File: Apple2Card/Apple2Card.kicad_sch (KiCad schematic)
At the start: 57 parts, among them J1 ICSP, J2 Conn_01x25, J3 Conn_01x25, J4 Conn_01x16, J5 SERCON, J6 WIZNET 5500, SW1 SW_Push, U1 ATmega328P-P, U3 74HCT00, U4 82C55A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

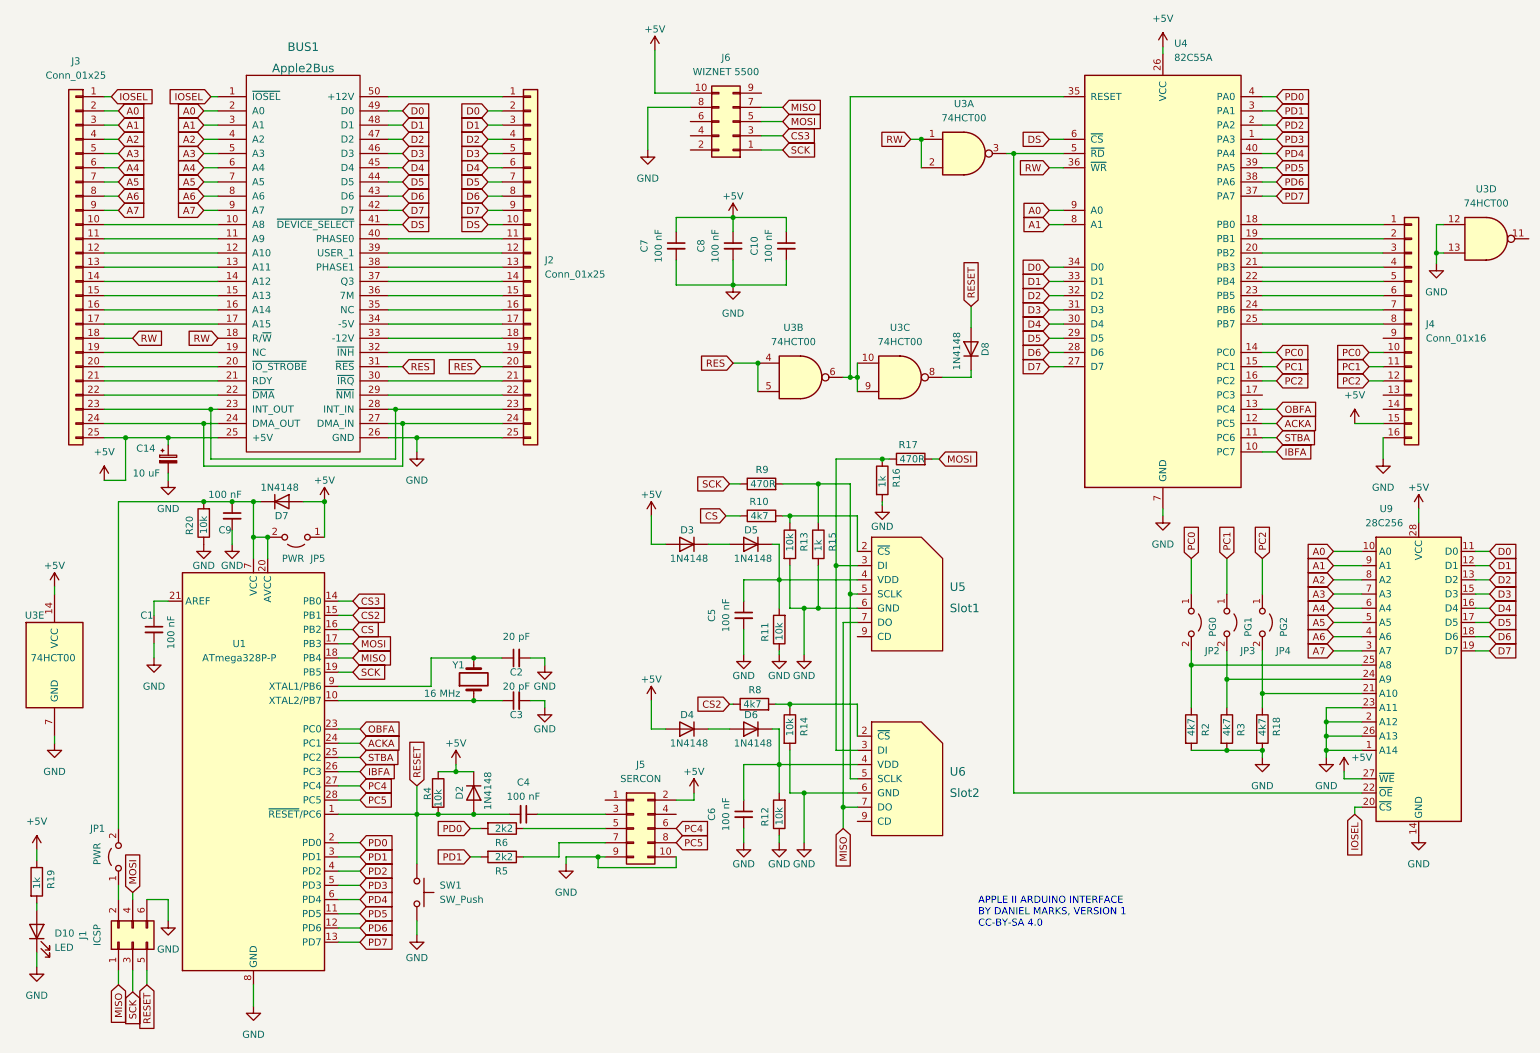
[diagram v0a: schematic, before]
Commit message: Fixed device select timing bug
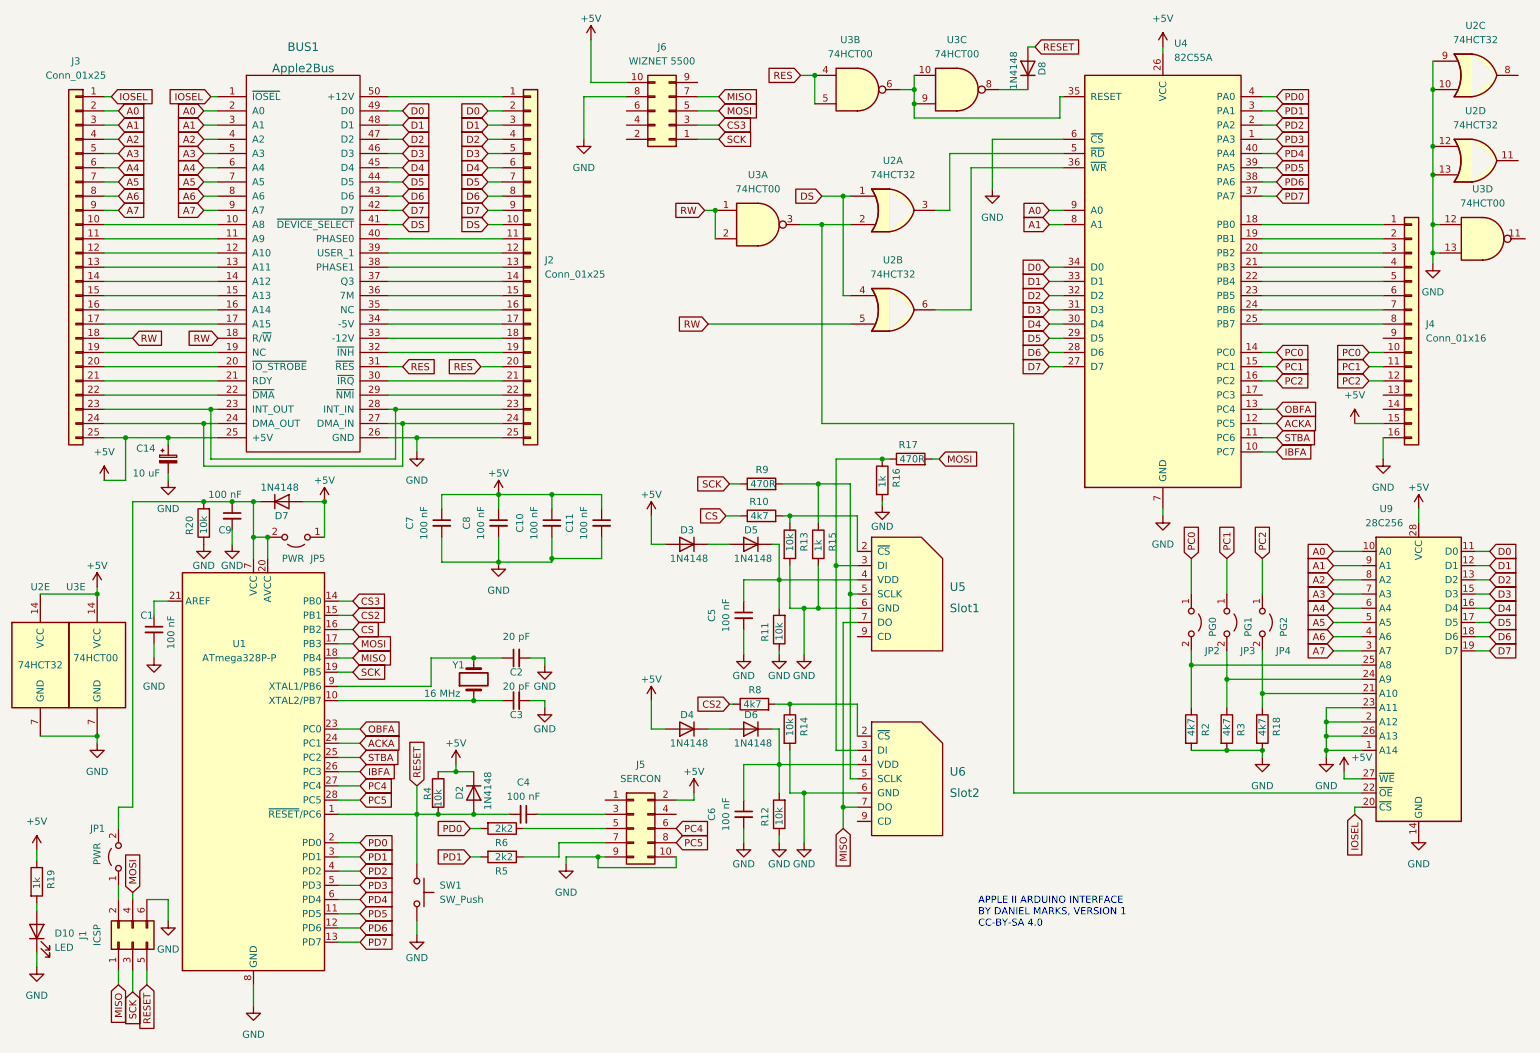
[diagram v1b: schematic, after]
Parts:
- added C11: 100 nF, Capacitor_THT:C_Disc_D5.0mm_W2.5mm_P5.00mm, symbol Device:C_Small
- added U2: 74HCT32, Package_DIP:DIP-14_W7.62mm_Socket, symbol 74xx:74LS32
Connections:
- net +5V: now also C11.1, U2.14 (VCC)
- net DS: now also U2.1, U2.4; no longer U4.6 (~{CS})
- net GND: now also U4.6 (~{CS}), C11.2, U2.10, U2.12, U2.13, U2.7 (GND), U2.9
- net RW: now also U2.5; no longer U4.36 (~{WR})
- net at U3.3, U9.22 (~{OE}): now also U2.2; no longer U4.5 (~{RD})
- new net: U2.3, U4.5 (~{RD})
- new net: U2.6, U4.36 (~{WR})
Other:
- moved on the sheet: C10, C7, C8, D8, J6, U3A, U3B, U3C, U3D, U3E

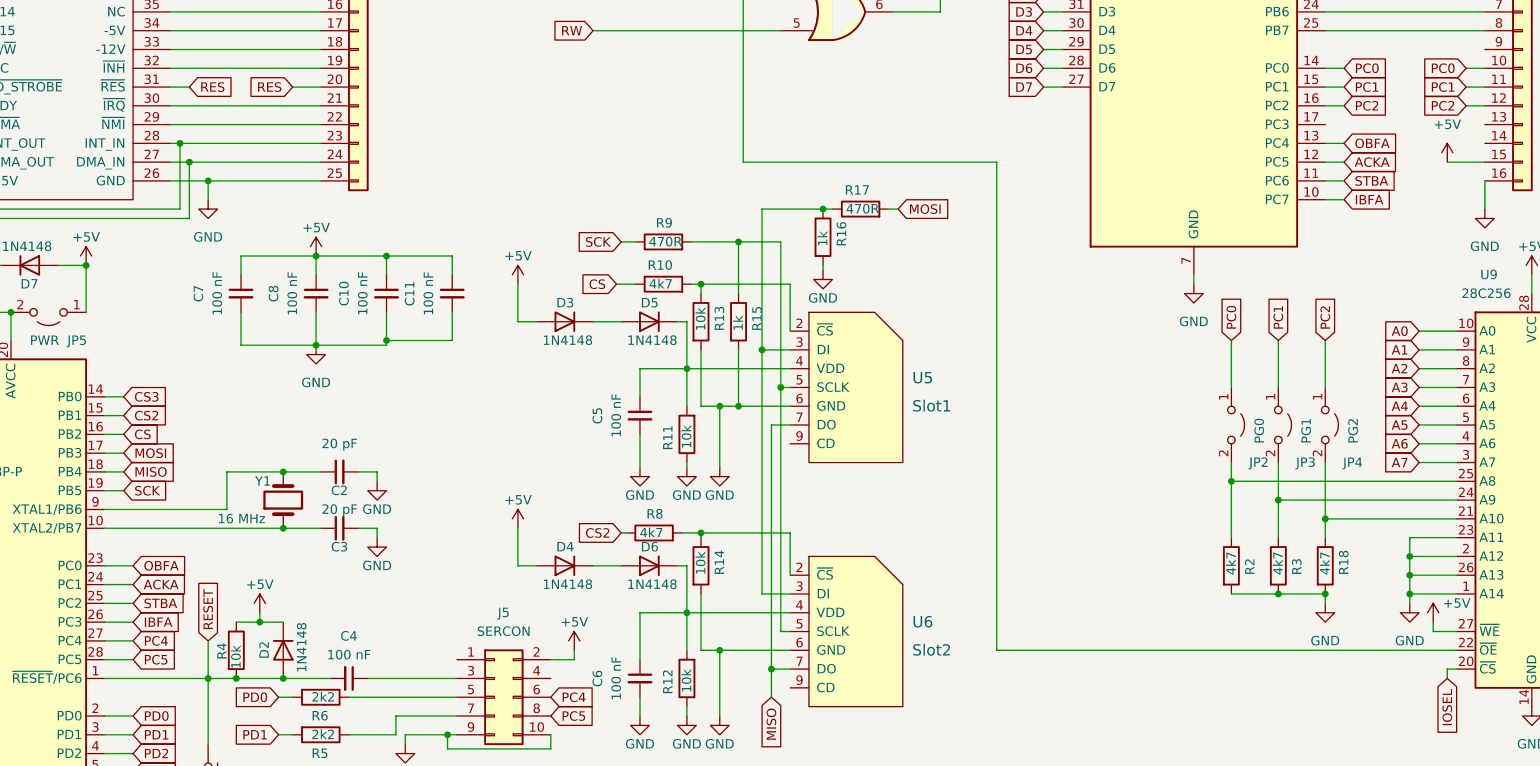
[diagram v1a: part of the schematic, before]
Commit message: Cards and storage works!
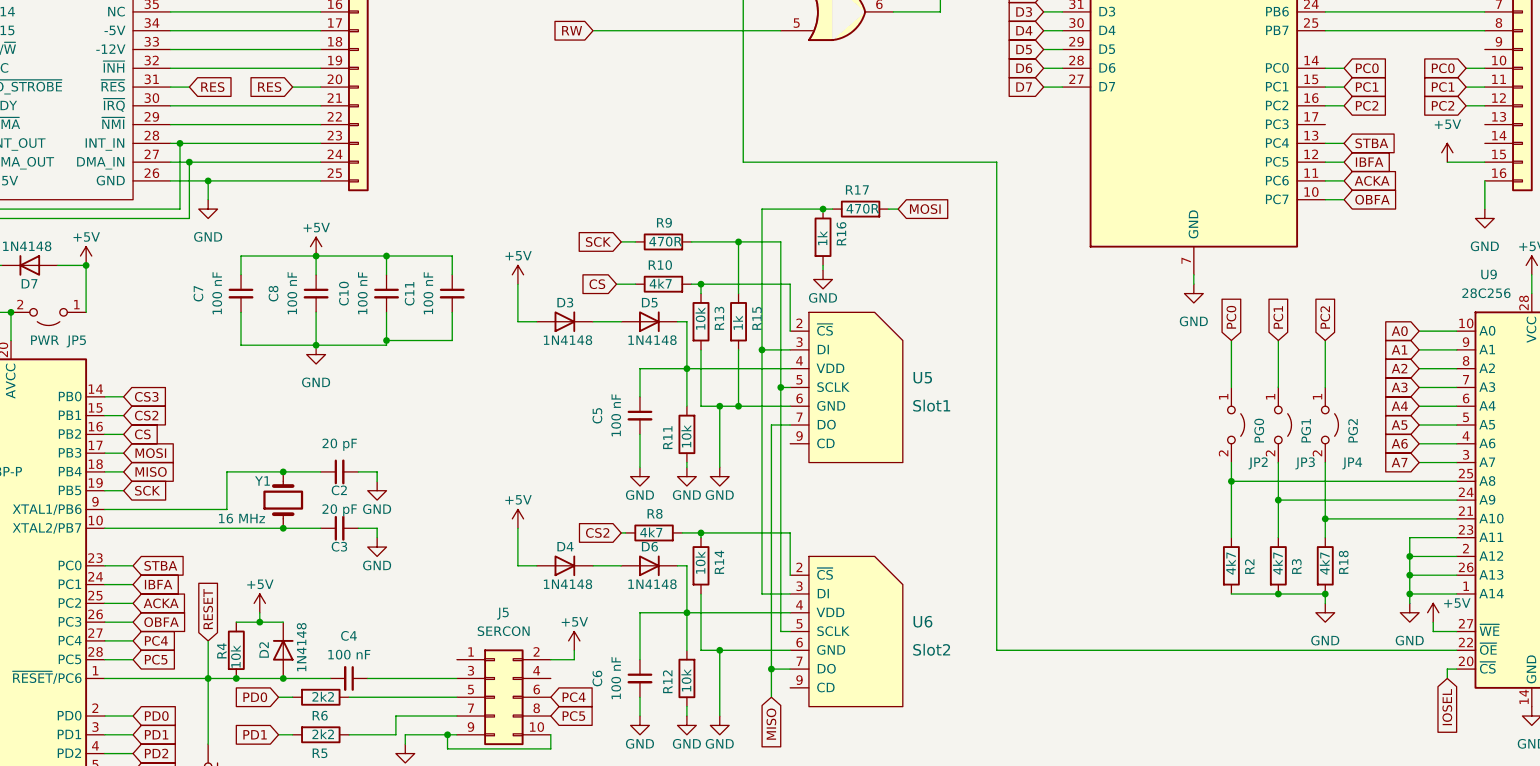
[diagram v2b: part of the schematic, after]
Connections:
- net ACKA: now also U1.25 (PC2), U4.11 (PC6); no longer U1.24 (PC1), U4.12 (PC5)
- net IBFA: now also U1.24 (PC1), U4.12 (PC5); no longer U1.26 (PC3), U4.10 (PC7)
- net OBFA: now also U1.26 (PC3), U4.10 (PC7); no longer U1.23 (PC0), U4.13 (PC4)
- net STBA: now also U1.23 (PC0), U4.13 (PC4); no longer U1.25 (PC2), U4.11 (PC6)
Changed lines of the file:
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@@
     )
   )
-  (global_label "ACKA" (shape input) (at 238.76 86.36 0) (fields_autoplaced)
-    (effects (font (size 1.27 1.27)) (justify left))
-    (property "Intersheet References" "${INTERSHEET_REFS}" (id 0) (at 245.8013 86.2806 0)
+  (global_label "ACKA" (shape input) (at 238.76 88.9 0) (fields_autoplaced)
+    (effects (font (size 1.27 1.27)) (justify left))
+    (property "Intersheet References" "${INTERSHEET_REFS}" (id 0) (at 245.8013 88.8206 0)
       (effects (font (size 1.27 1.27)) (justify left) hide)
     )
@@
     )
   )
-  (global_label "ACKA" (shape input) (at 74.93 143.51 0) (fields_autoplaced)
-    (effects (font (size 1.27 1.27)) (justify left))
-    (property "Intersheet References" "${INTERSHEET_REFS}" (id 0) (at 81.9713 143.4306 0)
-      (effects (font (size 1.27 1.27)) (justify left) hide)
-    )
-  )
-  (global_label "OBFA" (shape input) (at 74.93 140.97 0) (fields_autoplaced)
-    (effects (font (size 1.27 1.27)) (justify left))
-    (property "Intersheet References" "${INTERSHEET_REFS}" (id 0) (at 82.0318 140.8906 0)
+  (global_label "ACKA" (shape input) (at 74.93 146.05 0) (fields_autoplaced)
+    (effects (font (size 1.27 1.27)) (justify left))
+    (property "Intersheet References" "${INTERSHEET_REFS}" (id 0) (at 81.9713 145.9706 0)
+      (effects (font (size 1.27 1.27)) (justify left) hide)
+    )
+  )
+  (global_label "OBFA" (shape input) (at 74.93 148.59 0) (fields_autoplaced)
+    (effects (font (size 1.27 1.27)) (justify left))
+    (property "Intersheet References" "${INTERSHEET_REFS}" (id 0) (at 82.0318 148.5106 0)
       (effects (font (size 1.27 1.27)) (justify left) hide)
     )
@@
     )
   )
-  (global_label "IBFA" (shape input) (at 238.76 91.44 0) (fields_autoplaced)
-    (effects (font (size 1.27 1.27)) (justify left))
-    (property "Intersheet References" "${INTERSHEET_REFS}" (id 0) (at 245.1361 91.3606 0)
+  (global_label "IBFA" (shape input) (at 238.76 86.36 0) (fields_autoplaced)
+    (effects (font (size 1.27 1.27)) (justify left))
+    (property "Intersheet References" "${INTERSHEET_REFS}" (id 0) (at 245.1361 86.2806 0)
       (effects (font (size 1.27 1.27)) (justify left) hide)
     )
@@
     )
   )
-  (global_label "STBA" (shape input) (at 238.76 88.9 0) (fields_autoplaced)
-    (effects (font (size 1.27 1.27)) (justify left))
-    (property "Intersheet References" "${INTERSHEET_REFS}" (id 0) (at 245.6199 88.8206 0)
+  (global_label "STBA" (shape input) (at 238.76 83.82 0) (fields_autoplaced)
+    (effects (font (size 1.27 1.27)) (justify left))
+    (property "Intersheet References" "${INTERSHEET_REFS}" (id 0) (at 245.6199 83.7406 0)
       (effects (font (size 1.27 1.27)) (justify left) hide)
     )
@@
     )
   )
-  (global_label "IBFA" (shape input) (at 74.93 148.59 0) (fields_autoplaced)
-    (effects (font (size 1.27 1.27)) (justify left))
-    (property "Intersheet References" "${INTERSHEET_REFS}" (id 0) (at 81.3061 148.5106 0)
+  (global_label "IBFA" (shape input) (at 74.93 143.51 0) (fields_autoplaced)
+    (effects (font (size 1.27 1.27)) (justify left))
+    (property "Intersheet References" "${INTERSHEET_REFS}" (id 0) (at 81.3061 143.4306 0)
       (effects (font (size 1.27 1.27)) (justify left) hide)
     )
@@
     )
   )
-  (global_label "STBA" (shape input) (at 74.93 146.05 0) (fields_autoplaced)
-    (effects (font (size 1.27 1.27)) (justify left))
-    (property "Intersheet References" "${INTERSHEET_REFS}" (id 0) (at 81.7899 145.9706 0)
+  (global_label "STBA" (shape input) (at 74.93 140.97 0) (fields_autoplaced)
+    (effects (font (size 1.27 1.27)) (justify left))
+    (property "Intersheet References" "${INTERSHEET_REFS}" (id 0) (at 81.7899 140.8906 0)
       (effects (font (size 1.27 1.27)) (justify left) hide)
     )
@@
     )
   )
-  (global_label "OBFA" (shape input) (at 238.76 83.82 0) (fields_autoplaced)
-    (effects (font (size 1.27 1.27)) (justify left))
-    (property "Intersheet References" "${INTERSHEET_REFS}" (id 0) (at 245.8618 83.7406 0)
-      (effects (font (size 1.27 1.27)) (justify left) hide)
-    )
+  (global_label "OBFA" (shape input) (at 238.76 91.44 0) (fields_autoplaced)
+    (effects (font (size 1.27 1.27)) (justify left))
+    (property "Intersheet References" "${INTERSHEET_REFS}" (id 0) (at 245.8618 91.3606 0)
+      (effects (font (size 1.27 1.27)) (justify left) hide)
+    )
